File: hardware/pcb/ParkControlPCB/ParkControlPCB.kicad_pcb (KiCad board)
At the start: 2 copper layers, 3 parts, among them U1 LM1117-3.3, U2 ESP-12F

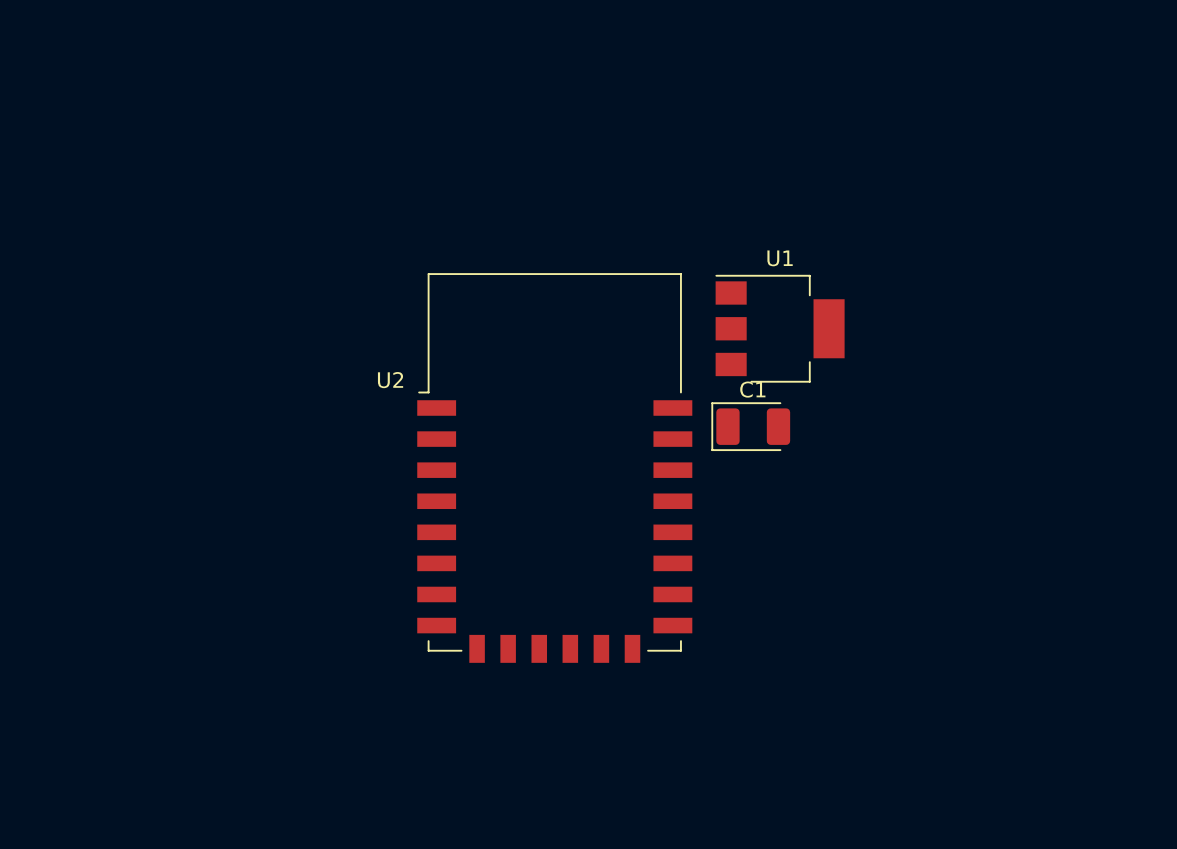
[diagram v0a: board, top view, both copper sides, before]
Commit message: Add power, spi, led and level shifter
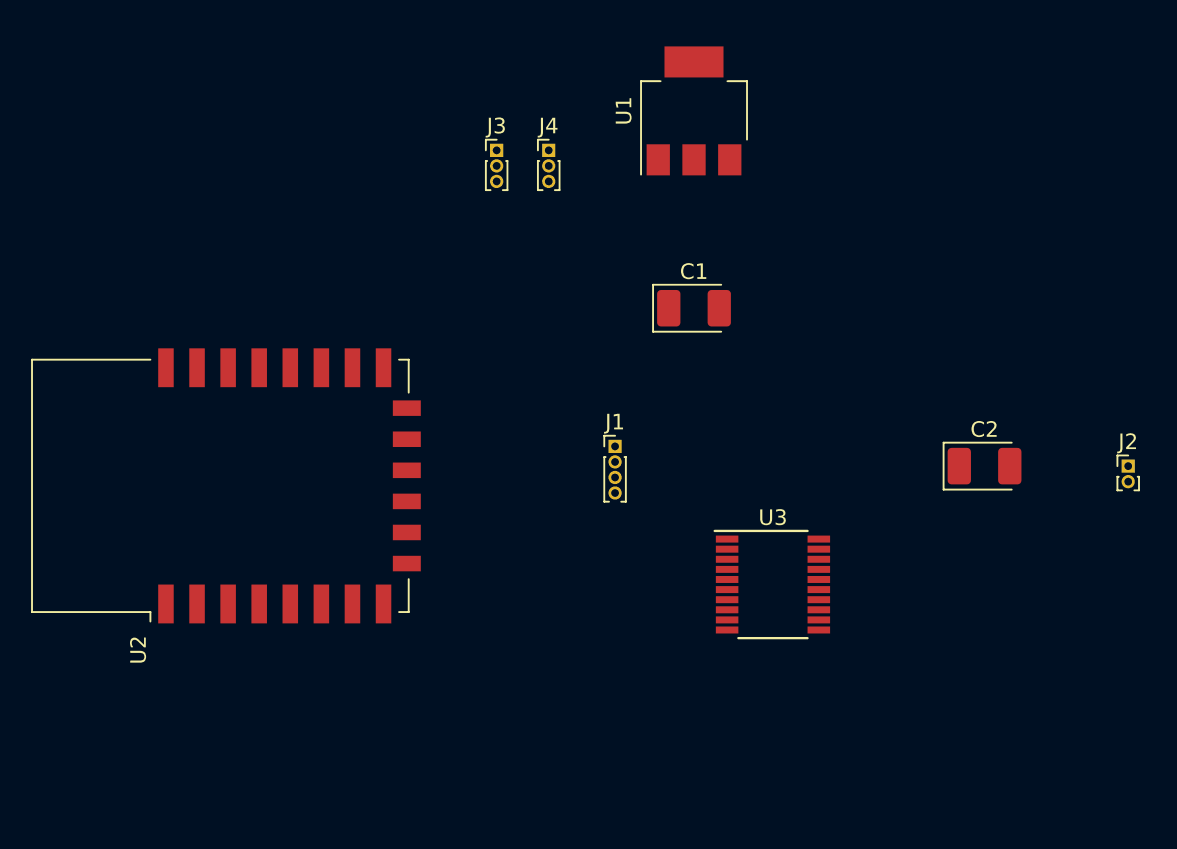
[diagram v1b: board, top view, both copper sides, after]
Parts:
- added C2: 1000 uF, 6,3V, Capacitor_Tantalum_SMD:CP_EIA-3528-12_Kemet-T_Pad1.50x2.35mm_HandSolder, F.Cu at (160.9, 92.7)
- added J1: Conn_01x04_Male, Connector_PinHeader_1.00mm:PinHeader_1x04_P1.00mm_Vertical, F.Cu at (137.2, 91.4)
- added J2: Conn_01x02_Male, Connector_PinHeader_1.00mm:PinHeader_1x02_P1.00mm_Vertical, F.Cu at (170.2, 92.7)
- added J3: Conn_01x03_Male, Connector_PinHeader_1.00mm:PinHeader_1x03_P1.00mm_Vertical, F.Cu at (129.5, 72.4)
- added J4: Conn_01x03_Male, Connector_PinHeader_1.00mm:PinHeader_1x03_P1.00mm_Vertical, F.Cu at (132.9, 72.4)
- added U3: TXS0108EPW, Package_SO:TSSOP-20_4.4x6.5mm_P0.65mm, F.Cu at (147.3, 100.3)
- moved U2 21.6 mm to (111.8, 94.0), turned to 90 degrees
- moved U1 15.1 mm to (142.2, 69.8), turned to 90 degrees
- moved C1 8.52 mm to (142.2, 82.5)
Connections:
- net /GND renamed GND
- U1 pad 3: /VCC -> VCC
- U2 pad 10: Net-(U2-Pad10) -> /MISO
- U2 pad 13: Net-(U2-Pad13) -> /MOSI
- U2 pad 14: Net-(U2-Pad14) -> /SCK
- U2 pad 9: Net-(U2-Pad9) -> /SS

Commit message: Added remaining pieces to schematics
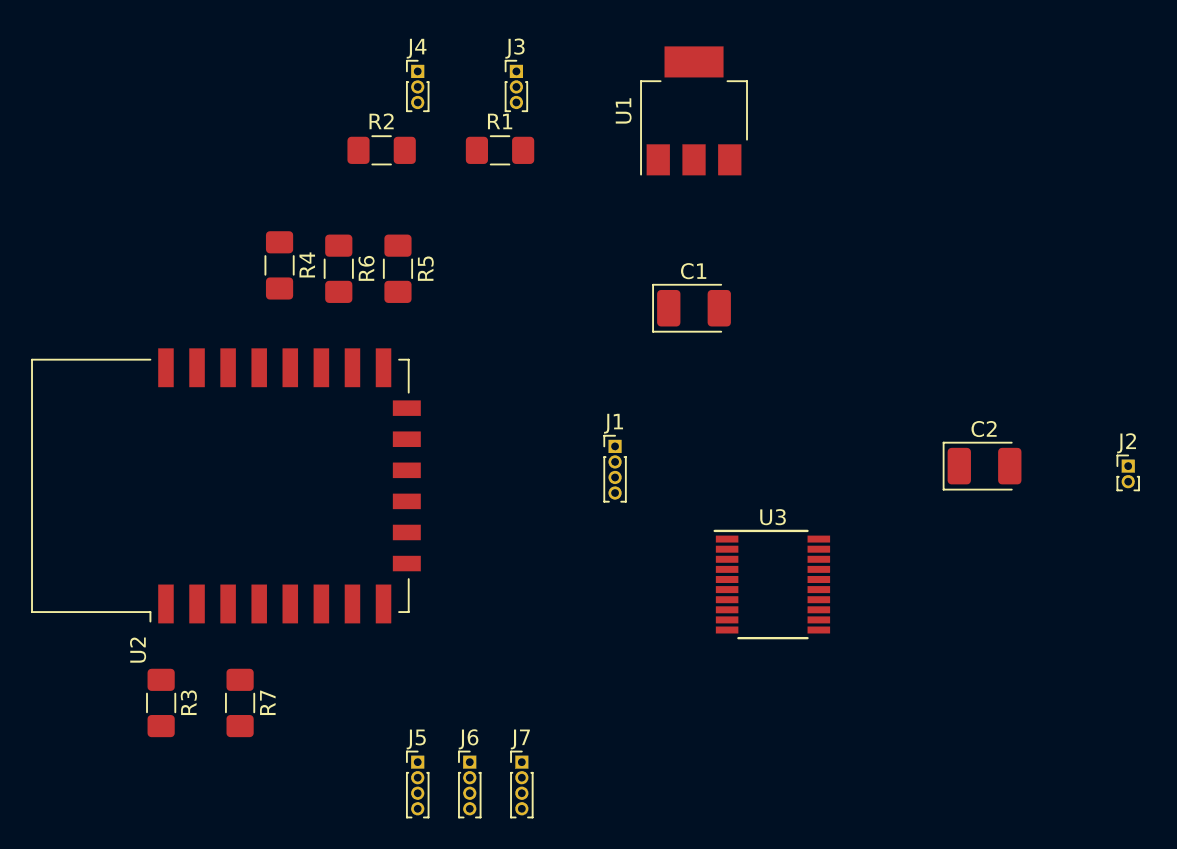
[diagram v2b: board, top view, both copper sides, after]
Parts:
- added J5: US1, Connector_PinHeader_1.00mm:PinHeader_1x04_P1.00mm_Vertical, F.Cu at (124.5, 111.8)
- added J6: US2, Connector_PinHeader_1.00mm:PinHeader_1x04_P1.00mm_Vertical, F.Cu at (127.8, 111.8)
- added J7: US3, Connector_PinHeader_1.00mm:PinHeader_1x04_P1.00mm_Vertical, F.Cu at (131.2, 111.8)
- added R1: 470, Resistor_SMD:R_1206_3216Metric_Pad1.42x1.75mm_HandSolder, F.Cu at (129.8, 72.4)
- added R2: 470, Resistor_SMD:R_1206_3216Metric_Pad1.42x1.75mm_HandSolder, F.Cu at (122.1, 72.4)
- added R3: 10K, Resistor_SMD:R_1206_3216Metric_Pad1.42x1.75mm_HandSolder, F.Cu at (108.0, 108.0)
- added R4: 10K, Resistor_SMD:R_1206_3216Metric_Pad1.42x1.75mm_HandSolder, F.Cu at (115.6, 79.8)
- added R5: 10K, Resistor_SMD:R_1206_3216Metric_Pad1.42x1.75mm_HandSolder, F.Cu at (123.2, 80.0)
- added R6: 10K, Resistor_SMD:R_1206_3216Metric_Pad1.42x1.75mm_HandSolder, F.Cu at (119.4, 80.0)
- added R7: 10K, Resistor_SMD:R_1206_3216Metric_Pad1.42x1.75mm_HandSolder, F.Cu at (113.0, 108.0)
- J1: value Conn_01x04_Male -> Prog
- J2: value Conn_01x02_Male -> PWR
- J3: value Conn_01x03_Male -> LED1
- J4: value Conn_01x03_Male -> LED2
- moved J4 9.84 mm to (124.5, 67.3)
- moved J3 5.24 mm to (130.8, 67.3)
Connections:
- J3 pad 2: /DIN_LED_1 -> Net-(J3-Pad2)
- J4 pad 2: /DIN_LED_2 -> Net-(J4-Pad2)
- U2 pad 11: Net-(U2-Pad11) -> /OE
- U2 pad 19: Net-(U2-Pad19) -> /US_T_1
- U2 pad 20: Net-(U2-Pad20) -> /US_E_1
- U2 pad 21: Net-(U2-Pad21) -> /LED_2
- U2 pad 22: Net-(U2-Pad22) -> /LED_1
- U2 pad 4: Net-(U2-Pad4) -> /US_E_3
- U2 pad 5: Net-(U2-Pad5) -> /US_T_3
- U2 pad 6: Net-(U2-Pad6) -> /US_T_2
- U2 pad 7: Net-(U2-Pad7) -> /US_E_2
- U3 pad 1: Net-(U3-Pad1) -> /LED_1
- U3 pad 10: Net-(U3-Pad10) -> /OE
- U3 pad 12: Net-(U3-Pad12) -> /US_E_3_5V
- U3 pad 13: Net-(U3-Pad13) -> /US_T_3_5V
- U3 pad 14: Net-(U3-Pad14) -> /US_E_2_5V
- U3 pad 15: Net-(U3-Pad15) -> /US_T_2_5V
- U3 pad 16: Net-(U3-Pad16) -> /US_E_1_5V
- U3 pad 17: Net-(U3-Pad17) -> /US_T_1_5V
- U3 pad 18: Net-(U3-Pad18) -> /DIN_LED_2
- U3 pad 20: Net-(U3-Pad20) -> /DIN_LED_1
- U3 pad 3: Net-(U3-Pad3) -> /LED_2
- U3 pad 4: Net-(U3-Pad4) -> /US_T_1
- U3 pad 5: Net-(U3-Pad5) -> /US_E_1
- U3 pad 6: Net-(U3-Pad6) -> /US_T_2
- U3 pad 7: Net-(U3-Pad7) -> /US_E_2
- U3 pad 8: Net-(U3-Pad8) -> /US_T_3
- U3 pad 9: Net-(U3-Pad9) -> /US_E_3

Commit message: Add net class for 4A conduits
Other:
- net class 4A Traces added: clearance 0.2, trace_width 2.1, via_dia 0.8, via_drill 0.4
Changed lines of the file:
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@@
     (add_net VCC)
+  )
+  (net_class "4A Traces" ""
+    (clearance 0.2)
+    (trace_width 2.1)
+    (via_dia 0.8)
+    (via_drill 0.4)
+    (uvia_dia 0.3)
+    (uvia_drill 0.1)
   )
   (module Connector_PinHeader_1.00mm:PinHeader_1x04_P1.00mm_Vertical (layer F.Cu)

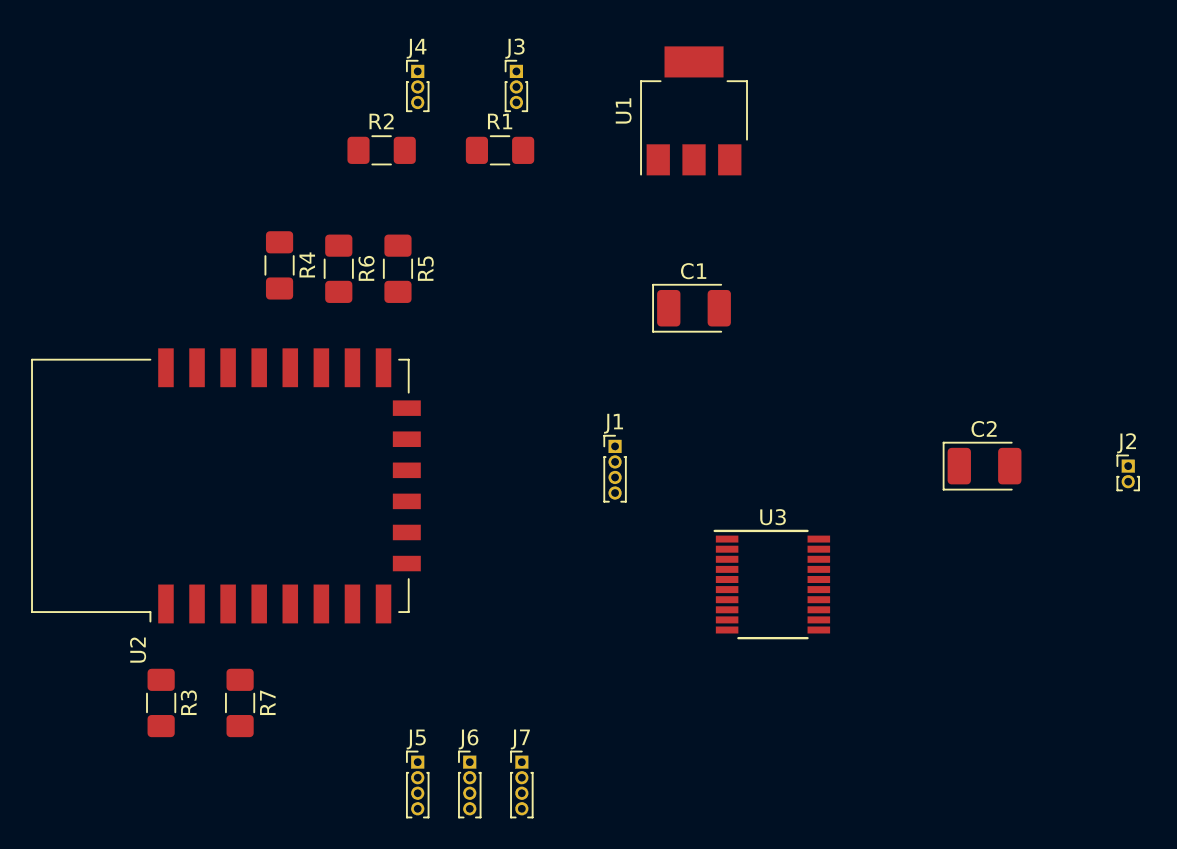
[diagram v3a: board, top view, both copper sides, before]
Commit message: Compact parts placement
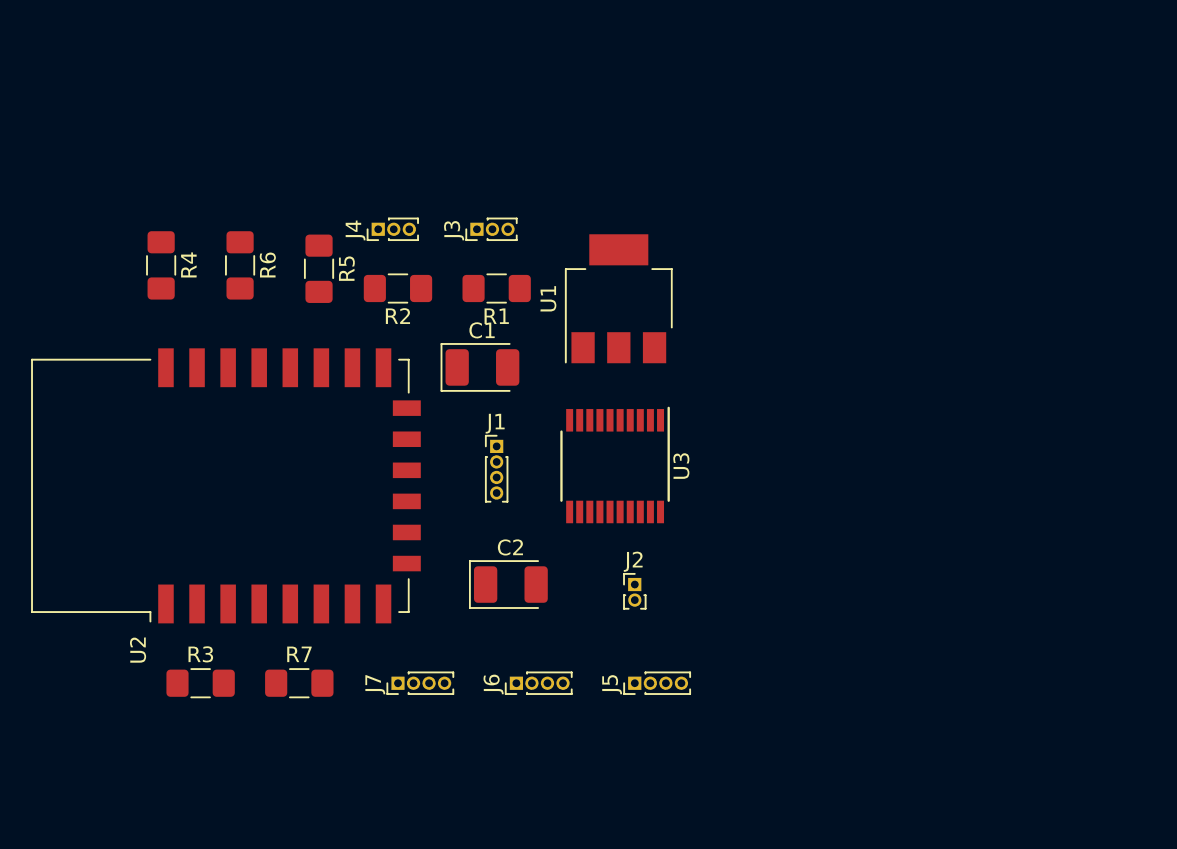
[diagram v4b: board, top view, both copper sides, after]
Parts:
- moved J2 32.7 mm to (138.4, 100.3)
- moved C2 31.4 mm to (130.5, 100.3)
- moved J5 14.9 mm to (138.4, 106.7), turned to 90 degrees
- moved C1 14.1 mm to (128.6, 86.4)
- moved U1 13.0 mm to (137.4, 81.9)
- moved U3 12.7 mm to (137.2, 92.7), turned to 270 degrees
- moved J3 10.5 mm to (128.3, 77.5), turned to 90 degrees
- moved J4 10.5 mm to (121.9, 77.5), turned to 90 degrees
- moved J7 9.45 mm to (123.2, 106.7), turned to 90 degrees
- moved R2 8.95 mm to (123.2, 81.3), turned to 180 degrees
- moved R1 8.89 mm to (129.5, 81.3), turned to 180 degrees
- moved J1 7.62 mm to (129.5, 91.4)
- moved R4 7.62 mm to (108.0, 79.8)
- moved R6 6.35 mm to (113.0, 79.8)
- moved J6 5.90 mm to (130.8, 106.7), turned to 90 degrees
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
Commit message: Some of the power circuits added
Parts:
- moved J2 21.9 mm to (142.2, 78.7)
- moved C2 21.7 mm to (137.2, 79.7), turned to 270 degrees
- moved C1 14.0 mm to (128.6, 100.3)
- moved U1 6.30 mm to (137.2, 88.2)
- moved U3 5.95 mm to (136.8, 98.7)
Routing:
- net GND: track 0.00 -> 125.7 mm, vias 0 -> 3
- net VCC: track 0.00 -> 121.4 mm, vias 0 -> 1
- net /3V3: track 0.00 -> 54.5 mm
- net Net-(R7-Pad1): track 0.00 -> 6.38 mm
- net Net-(R3-Pad1): track 0.00 -> 5.41 mm
